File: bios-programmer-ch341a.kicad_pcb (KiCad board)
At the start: 2 copper layers, 50 x 56 mm, 28 parts, among them J1 USB_B_Micro, J4 +Banana+, J5 -Banana-, J6 ZIF16, J7 Conn_02x04_Counter_Clockwise, J8 Conn_02x04_Counter_Clockwise, SW1 RESET, U1 CH341A, U2 ISO6741, U3 ADuM1252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

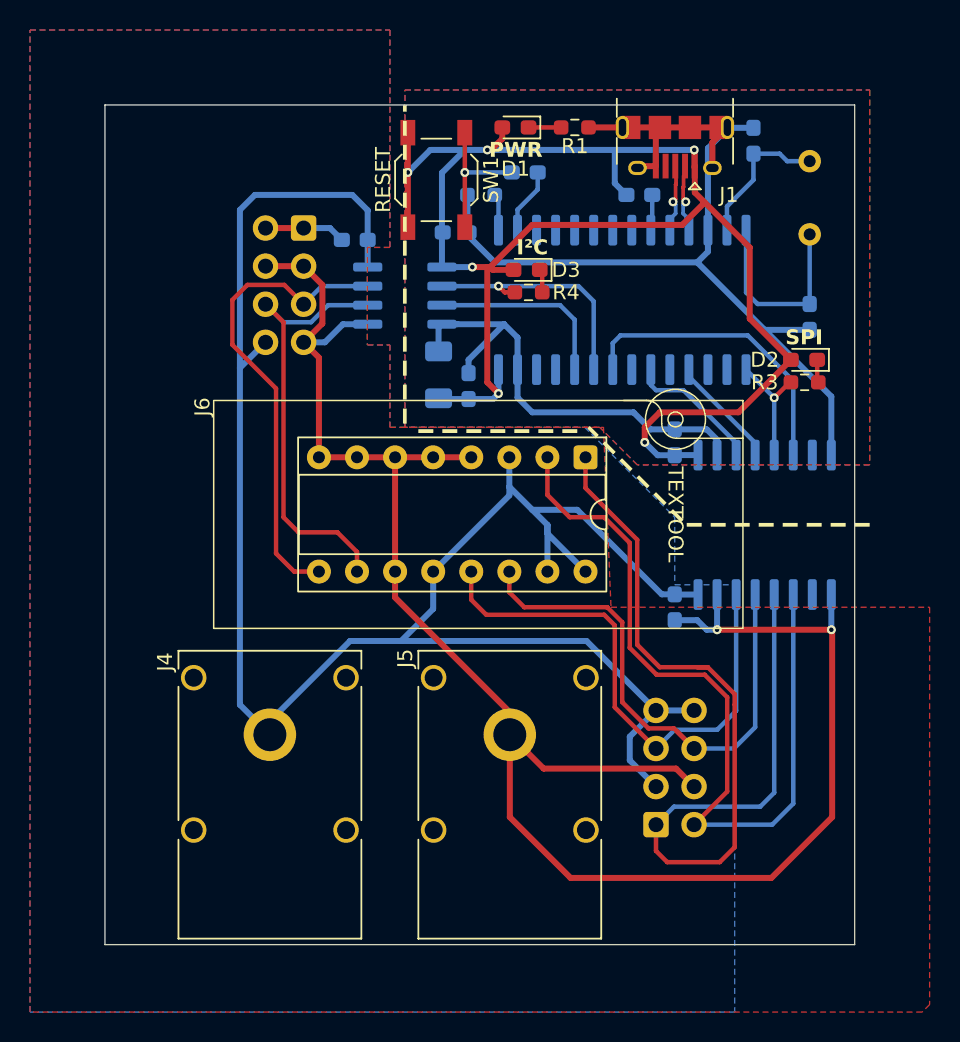
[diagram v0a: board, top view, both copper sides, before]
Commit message: PCB: routed VBUS at the bottom, GND on top
I tried it the other way around with VBUS on top and GND on the bottom side,
but this resulted in pretty annoying jumps & vias. This one is cleaner, there's
only one overjump to be made.
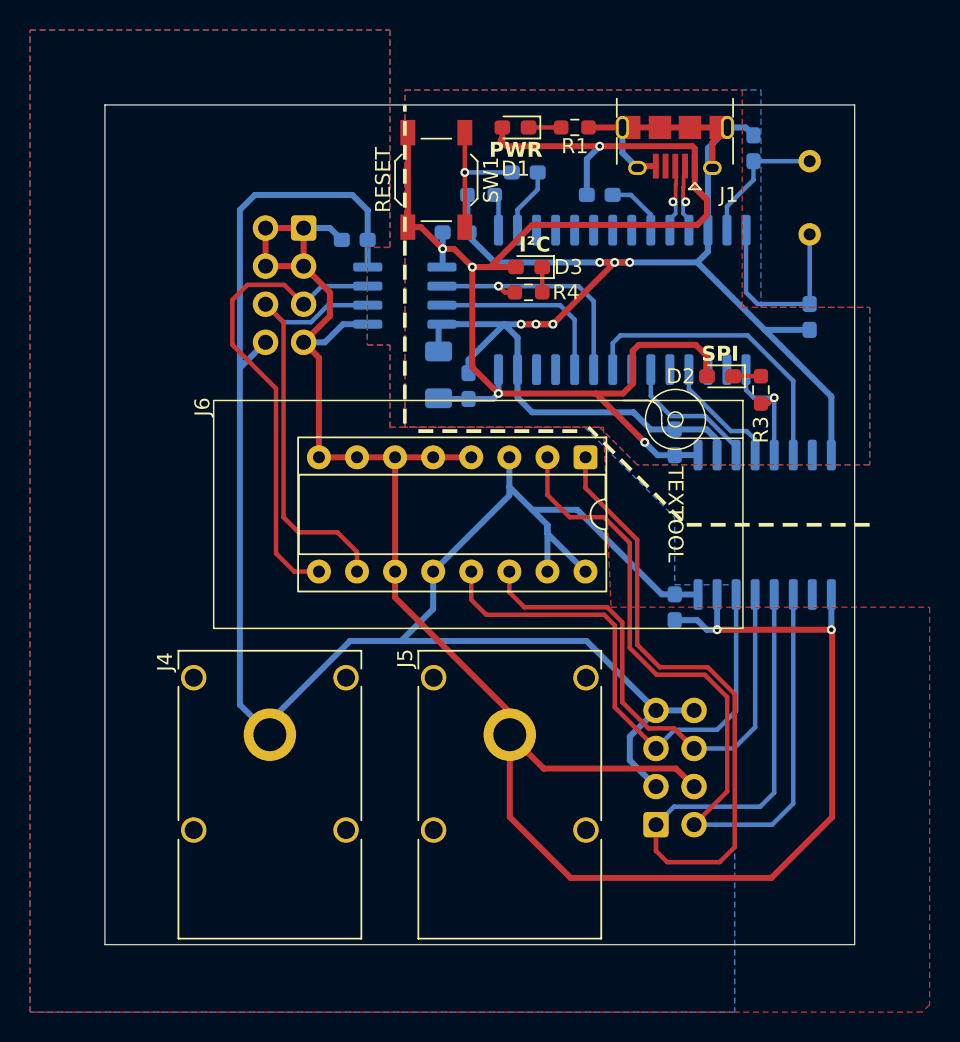
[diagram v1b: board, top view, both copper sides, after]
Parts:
- moved D2 5.71 mm to (81.0, 48.1)
- moved R3 2.96 mm to (83.8, 49.0), turned to 90 degrees
- moved C6 2.64 mm to (73.0, 36.0)
- moved C1 0.50 mm to (83.2, 32.9)
- moved D3 0.25 mm to (68.3, 40.8)
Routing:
- net GND: track 95.3 -> 109.8 mm, vias 0 -> 6
- net VBUS: track 108.2 -> 98.9 mm, vias 6 -> 5
- net GNDD: track 129.3 -> 134.8 mm
- net /CLK: track 6.25 -> 8.14 mm
- net /V3: track 2.26 -> 4.12 mm
- net Net-(U1-XI): track 9.79 -> 9.08 mm
- net /CS_I: track 62.4 -> 61.7 mm
- net /MOSI: track 8.31 -> 8.86 mm
- added copper zone on B.Cu, net GND
- added copper zone on F.Cu, net VBUS
- removed copper zone on F.Cu, net GND
- removed copper zone on B.Cu, net VBUS
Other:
- board text added: "reset switch kleiner ring rondom rond, niet connected? of toch GND? maar welke? 2 halve ringen? misschien beter 2 zones, tot bijna tegen elkaar?"
- board text removed: "TODO: ground plane op bovenkant, VBUS terug naar onder? reset switch kleiner ring rondom rond, niet connected? of toch GND? maar welke? 2 halve ringen? misschien beter 2 zones, tot bijna tegen elkaar?"

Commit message: PCB: moved ISO6741 more inwards
Originally pins for the socket came out much further since it was oriented
differently and - I think - I kept it this far to the side just by coincidence.
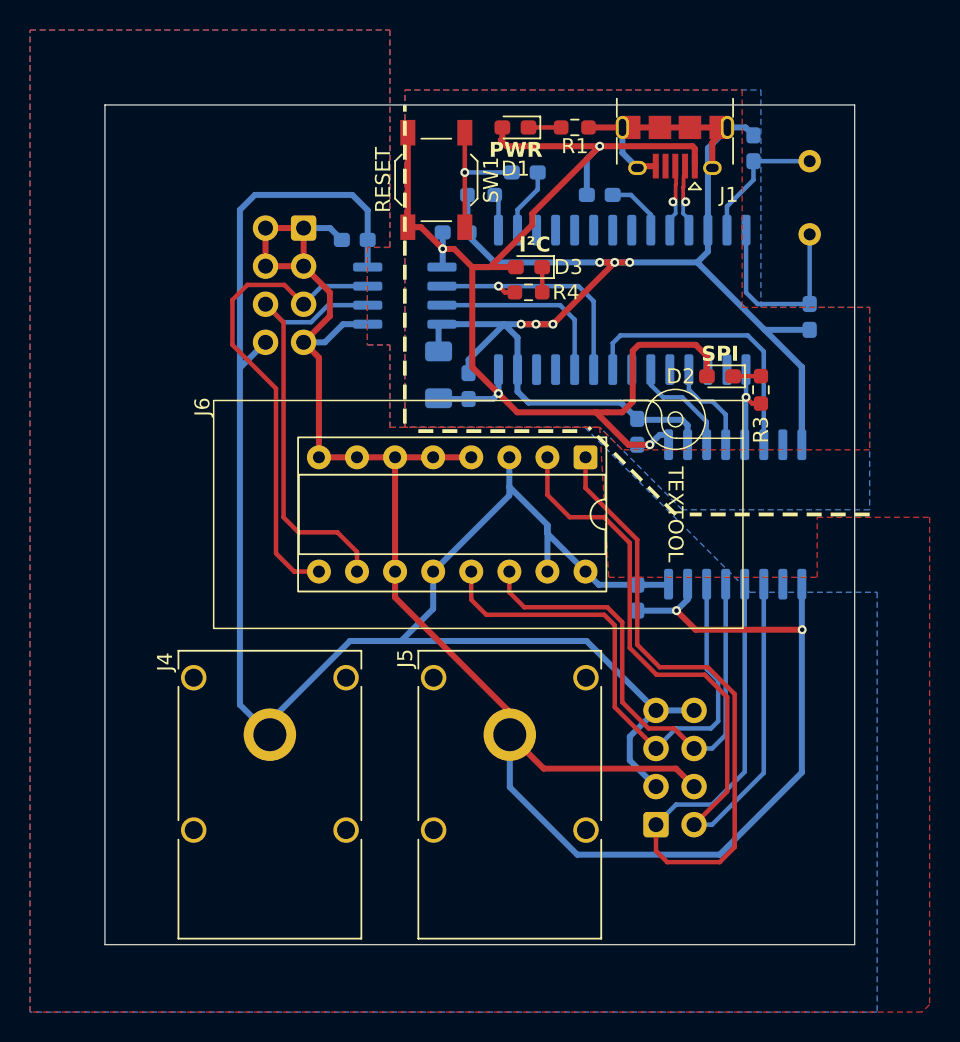
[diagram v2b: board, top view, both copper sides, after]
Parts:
- moved C8 2.60 mm to (75.5, 51.8)
- moved C9 2.58 mm to (75.5, 62.9)
- moved U2 2.08 mm to (82.0, 57.3)
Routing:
- net VBUS: track 98.9 -> 90.3 mm, vias 5 -> 4
- net VDD: track 129.8 -> 122.8 mm
- net GNDD: track 134.8 -> 129.8 mm
- net /MISO_I: track 54.8 -> 51.6 mm
- net /CS_I: track 61.7 -> 58.9 mm
- net GND: track 109.8 -> 111.9 mm
- net /CLK_I: track 36.3 -> 34.6 mm
- net /CLK: track 8.14 -> 6.49 mm
- net /MOSI: track 8.86 -> 7.30 mm
- net /CS: track 8.32 -> 6.81 mm
- net /MISO: track 20.2 -> 19.4 mm
- net /MOSI_I: track 35.7 -> 35.1 mm

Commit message: PCB: ring of fire; grounded vias around the pcb to improve signal integrity.
This is something I saw on the black version of the CH341 programmer and I
wanted to try out laying this out as well.

The green versions that I have - which have a voltage selection switch - do not
have such a ring and they work perfectly fine (with the limitations of these
simple devices). Not sure if it's useful at all thus, but I'm going to assume
that it doesn't harm anything. Let's hope these aren't going to be famous last
words.

Having added this it's clear that there is quite a bit of extra surface area
that hasn't been used nor has any use. So if I decide to remove this ring at a
later stage, I might just reclaim that area instead of making it empty.

Thank you Johnny Cash for making me remember "Ring of Fire" just when I was
laying this out.
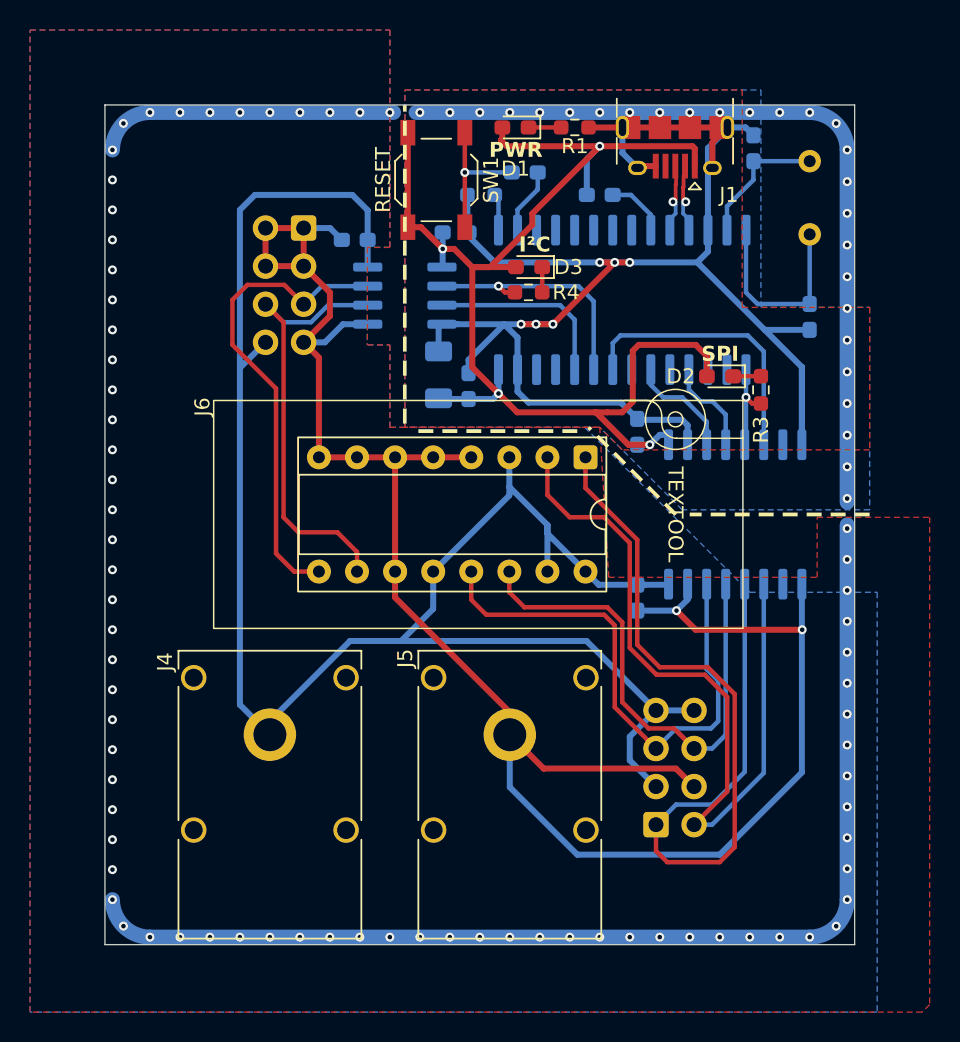
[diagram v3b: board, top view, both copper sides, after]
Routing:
- net GNDD: track 129.8 -> 276.5 mm, vias 2 -> 76
- net GND: track 111.9 -> 165.4 mm, vias 6 -> 33

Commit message: PCB: components moved inside Ring of Fire + fixed grouping & locking
While I will never know if this ring around the PCB has any merit, it does mean
that some of the components had to move a bit. No issues created as far as I
can see.

The grouping that I had done was apparently messed up, so I've had to redo this
by moving them to the side and finally grouping, moving back & locking them.
Note sure if it was messed up because of a bug or by design - or something I
did wrong.
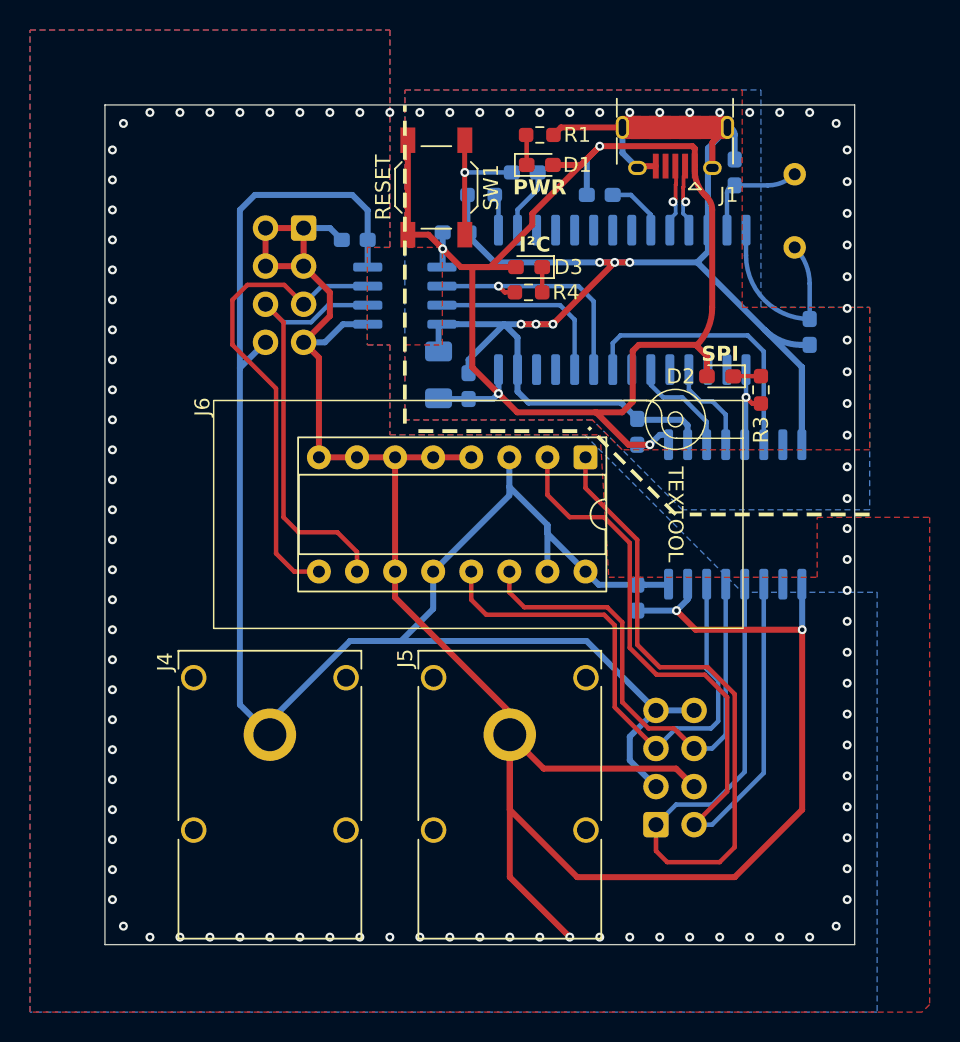
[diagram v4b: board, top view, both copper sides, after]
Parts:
- moved D1 2.98 mm to (69.0, 34.0), turned to 0 degrees
- moved R1 2.39 mm to (69.0, 32.0)
- moved C1 2.04 mm to (82.0, 34.5)
- moved Y1 1.33 mm to (86.0, 39.5)
- moved C2 1.00 mm to (87.0, 45.1)
- moved SW1 0.50 mm to (62.1, 35.5)
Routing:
- net GNDD: track 276.5 -> 442.0 mm
- net GND: track 165.4 -> 222.2 mm
- net VBUS: track 90.3 -> 97.9 mm
- net /RST: track 9.44 -> 15.7 mm
- net Net-(U1-XI): track 9.08 -> 7.45 mm

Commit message: PCB/footprints: Replaced reset switch with a smaller (and cheaper) model
C&K PTS636 is also already in Kicad, it's affordable and should be more than
enough for this simple board.
More notably it's rectangular and takes up less space than the big one I had
before. I do like that one better, but it's a bit big for this board.
Now it'll also be possible to have it all on the - unofficially - isolated side
of the pcb.
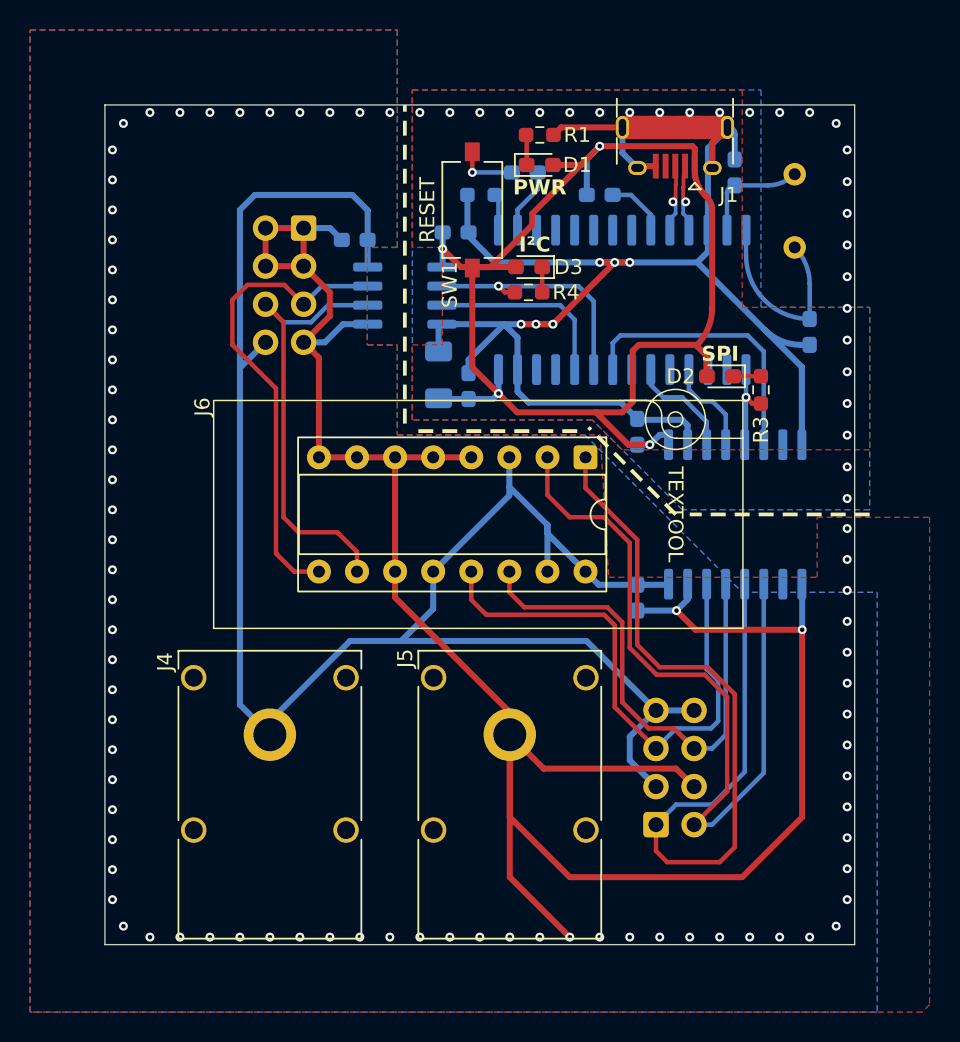
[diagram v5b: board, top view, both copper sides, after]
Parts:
- SW1: footprint Button_Switch_SMD:SW_SPST_TL3342 -> Button_Switch_SMD:SW_Tactile_SPST_NO_Straight_CK_PTS636Sx25SMTRLFS
- moved SW1 2.83 mm to (64.5, 37.0)
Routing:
- net /RST: track 15.7 -> 4.01 mm
- net VBUS: track 97.9 -> 88.9 mm
- net GNDD: track 442.0 -> 442.6 mm

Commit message: PCB: so satisfying ... rounded some tracks just because I can :)
Yeah, I shouldn't ben doing this since it's strictly not necessary. But just
imagine all these electronics moving at light speed and then bumping again a
sharp corner! They might hurt themselves, possibly leading to a universe-ending
event. Or not.
Technically I'm pretty sure I read a application note or something about it
once, but I'm also pretty sure that all of this has happened before at least
once. So yeah, fun life, right?
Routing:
- net VDD: track 122.8 -> 142.0 mm
- net /SCL_I: track 29.7 -> 27.0 mm
- net /CLK_I: track 34.6 -> 32.1 mm
- net /SDA_I: track 32.0 -> 30.6 mm
- net GNDD: track 442.6 -> 443.6 mm
